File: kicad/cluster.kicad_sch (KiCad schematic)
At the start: 17 parts, among them J1 Conn_01x07

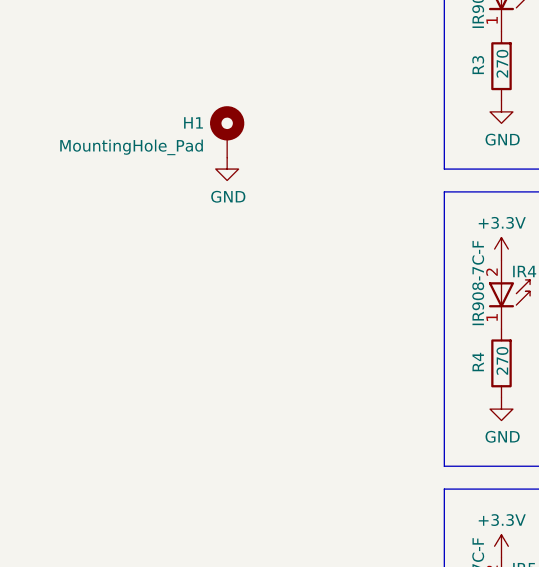
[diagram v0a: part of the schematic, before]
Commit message: Initial commit of lalboard extended features, including breakout board.
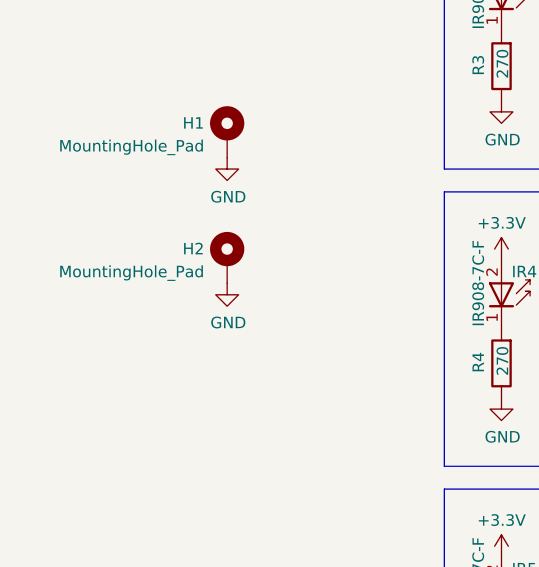
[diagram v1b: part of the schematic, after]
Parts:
- added H2: MountingHole_Pad, MountingHole:MountingHole_2.2mm_M2_DIN965_Pad, symbol Mechanical:MountingHole_Pad
- H1: footprint MountingHole:MountingHole_3.2mm_M3_DIN965_Pad -> MountingHole:MountingHole_2.2mm_M2_DIN965_Pad
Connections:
- net GND: now also H2.1
